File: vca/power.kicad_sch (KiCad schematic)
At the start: 16 parts, among them U16 power_conn_16, U18 LM7805_TO220, U19 ZLDO1117G33TA

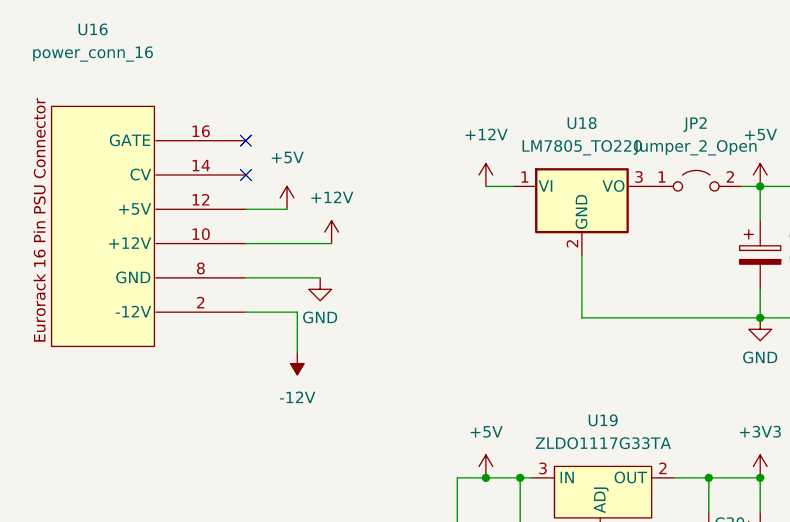
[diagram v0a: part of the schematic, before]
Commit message: added LEDs to LUM
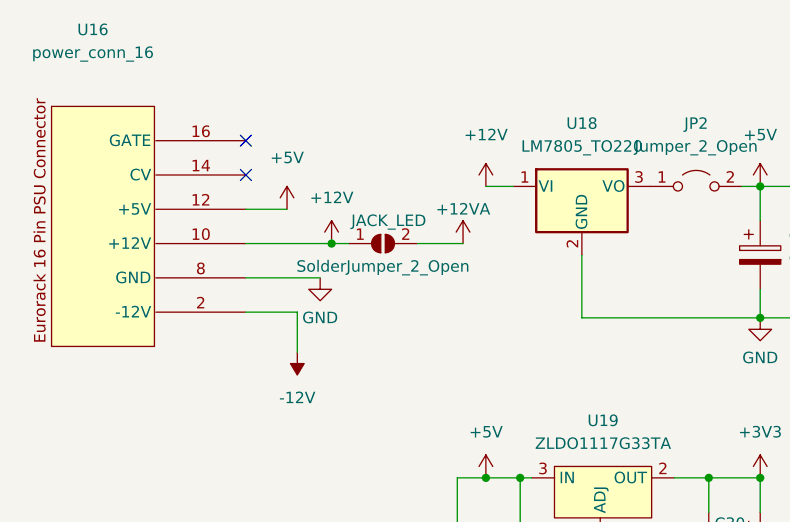
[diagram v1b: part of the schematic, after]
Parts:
- added JACK_LED: SolderJumper_2_Open, symbol Jumper:SolderJumper_2_Open
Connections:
- net +12V: now also JACK_LED.1 (A)
- new net +12VA: JACK_LED.2 (B)
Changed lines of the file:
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@@
   (junction (at 104.14 60.96) (diameter 0) (color 0 0 0 0)
+  )
+  (junction (at 62.23 34.925) (diameter 0) (color 0 0 0 0)
   )
   (junction (at 82.55 107.95) (diameter 0) (color 0 0 0 0)
@@
   )
   (wire (pts (xy 109.855 28.575) (xy 133.985 28.575))
+    (stroke (width 0) (type default) (color 0 0 0 0))
+  )
+  (wire (pts (xy 71.755 34.925) (xy 76.835 34.925))
+    (stroke (width 0) (type default) (color 0 0 0 0))
+  )
+  (wire (pts (xy 62.23 34.925) (xy 64.135 34.925))
     (stroke (width 0) (type default) (color 0 0 0 0))
   )
@@
     (pin "2")
   )
+  (symbol (lib_id "power:+12VA") (at 76.835 34.925 0) (unit 1)
+    (in_bom yes) (on_board yes)
+    (property "Reference" "#PWR?" (id 0) (at 76.835 38.735 0)
+      (effects (font (size 1.27 1.27)) hide)
+    )
+    (property "Value" "+12VA" (id 1) (at 76.835 31.115 0))
+    (property "Footprint" "" (id 2) (at 76.835 34.925 0)
+      (effects (font (size 1.27 1.27)) hide)
+    )
+    (property "Datasheet" "" (id 3) (at 76.835 34.925 0)
+      (effects (font (size 1.27 1.27)) hide)
+    )
+    (pin "1")
+  )
   (symbol (lib_id "eurorack:C-100nF-0805") (at 83.185 69.85 0) (unit 1)
     (in_bom yes) (on_board yes)
@@
     (pin "1")
   )
+  (symbol (lib_id "Jumper:SolderJumper_2_Open") (at 67.945 34.925 0) (unit 1)
+    (in_bom yes) (on_board yes)
+    (property "Reference" "JACK_LED" (id 0) (at 68.58 32.385 0))
+    (property "Value" "SolderJumper_2_Open" (id 1) (at 67.945 37.465 0))
+    (property "Footprint" "" (id 2) (at 67.945 34.925 0)
+      (effects (font (size 1.27 1.27)) hide)
+    )
+    (property "Datasheet" "~" (id 3) (at 67.945 34.925 0)
+      (effects (font (size 1.27 1.27)) hide)
+    )
+    (pin "1")
+    (pin "2")
+  )
   (symbol (lib_id "eurorack:C-100nF-0805") (at 71.755 93.98 0) (unit 1)

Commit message: some fixes, starting to work on PCB
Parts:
- JACK_LED1: renamed from JACK_LED; footprint (none) -> Jumper:SolderJumper-2_P1.3mm_Open_Pad1.0x1.5mm
- gave numbers to parts that had none: 2
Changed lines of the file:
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@@
   (symbol (lib_id "power:+12VA") (at 76.835 34.925 0) (unit 1)
     (in_bom yes) (on_board yes)
-    (property "Reference" "#PWR?" (id 0) (at 76.835 38.735 0)
+    (property "Reference" "#PWR0128" (id 0) (at 76.835 38.735 0)
       (effects (font (size 1.27 1.27)) hide)
     )
@@
   (symbol (lib_id "power:+5V") (at 155.575 62.865 0) (unit 1)
     (in_bom yes) (on_board yes) (fields_autoplaced)
-    (property "Reference" "#PWR?" (id 0) (at 155.575 66.675 0)
+    (property "Reference" "#PWR0126" (id 0) (at 155.575 66.675 0)
       (effects (font (size 1.27 1.27)) hide)
     )
@@
   (symbol (lib_id "Device:LED") (at 155.575 77.47 90) (unit 1)
     (in_bom yes) (on_board yes) (fields_autoplaced)
-    (property "Reference" "D?" (id 0) (at 158.75 77.7874 90)
+    (property "Reference" "D2" (id 0) (at 158.75 77.7874 90)
       (effects (font (size 1.27 1.27)) (justify right))
     )
@@
   (symbol (lib_id "eurorack:R-470-1206") (at 155.575 67.945 0) (unit 1)
     (in_bom yes) (on_board yes) (fields_autoplaced)
-    (property "Reference" "R?" (id 0) (at 157.48 66.6749 0)
+    (property "Reference" "R7" (id 0) (at 157.48 66.6749 0)
       (effects (font (size 1.27 1.27)) (justify left))
     )
@@
   (symbol (lib_id "Jumper:SolderJumper_2_Open") (at 67.945 34.925 0) (unit 1)
     (in_bom yes) (on_board yes)
-    (property "Reference" "JACK_LED" (id 0) (at 68.58 32.385 0))
+    (property "Reference" "JACK_LED1" (id 0) (at 68.58 32.385 0))
     (property "Value" "SolderJumper_2_Open" (id 1) (at 67.945 37.465 0))
-    (property "Footprint" "" (id 2) (at 67.945 34.925 0)
+    (property "Footprint" "Jumper:SolderJumper-2_P1.3mm_Open_Pad1.0x1.5mm" (id 2) (at 67.945 34.925 0)
       (effects (font (size 1.27 1.27)) hide)
     )
@@
   (symbol (lib_id "power:GND") (at 155.575 83.185 0) (unit 1)
     (in_bom yes) (on_board yes) (fields_autoplaced)
-    (property "Reference" "#PWR?" (id 0) (at 155.575 89.535 0)
-      (effects (font (size 1.27 1.27)) hide)
-    )
+    (property "Reference" "#PWR0127" (id 0) (at 155.575 89.535 0)
+      (effects (font (size 1.27 1.27)) hide)
+    )

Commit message: working on the back panel power section
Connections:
- net +5V: no longer C21.1
- net at JP2.1 (A), U18.3 (VO): now also C21.1
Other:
- moved on the sheet: JP2
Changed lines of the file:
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@@
 (kicad_sch (version 20211123) (generator eeschema)
   (paper "A4")
+  (junction (at 97.79 28.575) (diameter 0) (color 0 0 0 0)
+  )
   (junction (at 109.855 43.18) (diameter 0) (color 0 0 0 0)
   )
@@
   )
   (junction (at 77.47 99.06) (diameter 0) (color 0 0 0 0)
+  )
+  (junction (at 97.663 28.575) (diameter 0) (color 0 0 0 0)
   )
   (junction (at 83.185 60.96) (diameter 0) (color 0 0 0 0)
@@
     (stroke (width 0) (type default) (color 0 0 0 0))
   )
+  (wire (pts (xy 98.425 28.575) (xy 97.79 28.575))
+    (stroke (width 0) (type default) (color 0 0 0 0))
+  )
   (wire (pts (xy 100.33 60.96) (xy 104.14 60.96))
     (stroke (width 0) (type default) (color 0 0 0 0))
@@
     (stroke (width 0) (type default) (color 0 0 0 0))
   )
-  (wire (pts (xy 107.823 28.575) (xy 109.855 28.575))
+  (wire (pts (xy 108.585 28.575) (xy 109.855 28.575))
     (stroke (width 0) (type default) (color 0 0 0 0))
   )
@@
     (stroke (width 0) (type default) (color 0 0 0 0))
   )
-  (wire (pts (xy 109.855 28.575) (xy 109.855 32.385))
+  (wire (pts (xy 109.855 32.385) (xy 97.79 32.385))
     (stroke (width 0) (type default) (color 0 0 0 0))
   )
@@
     (stroke (width 0) (type default) (color 0 0 0 0))
   )
+  (wire (pts (xy 97.79 28.575) (xy 97.79 32.385))
+    (stroke (width 0) (type default) (color 0 0 0 0))
+  )
   (wire (pts (xy 104.14 64.77) (xy 104.14 60.96))
     (stroke (width 0) (type default) (color 0 0 0 0))
   )
   (wire (pts (xy 71.755 90.17) (xy 71.755 88.9))
+    (stroke (width 0) (type default) (color 0 0 0 0))
+  )
+  (wire (pts (xy 97.79 28.575) (xy 97.663 28.575))
     (stroke (width 0) (type default) (color 0 0 0 0))
   )
@@
     (pin "2")
   )
-  (symbol (lib_id "Jumper:Jumper_2_Open") (at 102.743 28.575 0) (unit 1)
-    (in_bom yes) (on_board yes) (fields_autoplaced)
-    (property "Reference" "JP2" (id 0) (at 102.743 21.59 0))
-    (property "Value" "Jumper_2_Open" (id 1) (at 102.743 24.13 0))
-    (property "Footprint" "Jumper:SolderJumper-2_P1.3mm_Open_Pad1.0x1.5mm" (id 2) (at 102.743 28.575 0)
-      (effects (font (size 1.27 1.27)) hide)
-    )
-    (property "Datasheet" "~" (id 3) (at 102.743 28.575 0)
-      (effects (font (size 1.27 1.27)) hide)
-    )
+  (symbol (lib_id "Jumper:Jumper_2_Open") (at 103.505 28.575 0) (unit 1)
+    (in_bom yes) (on_board yes) (fields_autoplaced)
+    (property "Reference" "JP2" (id 0) (at 103.505 21.59 0))
+    (property "Value" "Jumper_2_Open" (id 1) (at 103.505 24.13 0))
+    (property "Footprint" "Jumper:SolderJumper-2_P1.3mm_Open_Pad1.0x1.5mm" (id 2) (at 103.505 28.575 0)
+      (effects (font (size 1.27 1.27)) hide)
+    )
+    (property "Datasheet" "~" (id 3) (at 103.505 28.575 0)
+      (effects (font (size 1.27 1.27)) hide)
+    )

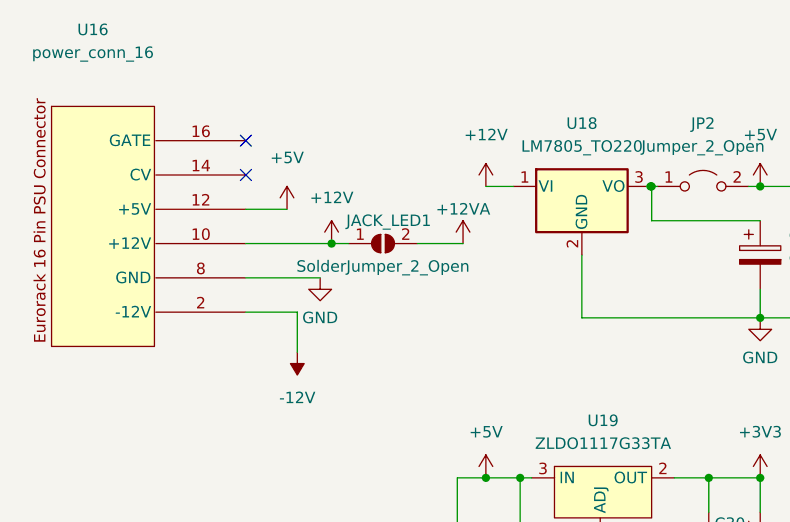
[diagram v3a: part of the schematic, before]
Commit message: Fixed some pins on the connectors, and working on the back board, power left to go
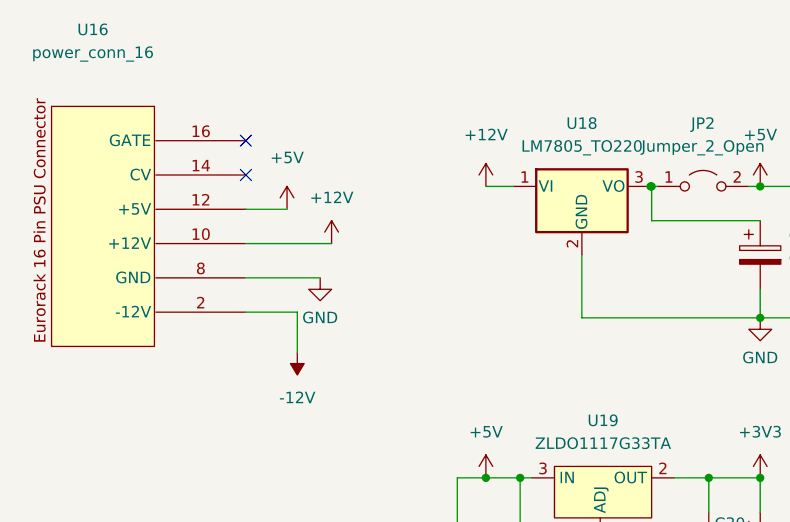
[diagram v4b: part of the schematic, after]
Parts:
- removed JACK_LED1: SolderJumper_2_Open, Jumper:SolderJumper-2_P1.3mm_Open_Pad1.0x1.5mm, symbol Jumper:SolderJumper_2_Open
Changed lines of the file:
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@@
   (junction (at 104.14 60.96) (diameter 0) (color 0 0 0 0)
-  )
-  (junction (at 62.23 34.925) (diameter 0) (color 0 0 0 0)
   )
   (junction (at 82.55 107.95) (diameter 0) (color 0 0 0 0)
@@
   )
   (wire (pts (xy 109.855 28.575) (xy 133.985 28.575))
-    (stroke (width 0) (type default) (color 0 0 0 0))
-  )
-  (wire (pts (xy 71.755 34.925) (xy 76.835 34.925))
-    (stroke (width 0) (type default) (color 0 0 0 0))
-  )
-  (wire (pts (xy 62.23 34.925) (xy 64.135 34.925))
     (stroke (width 0) (type default) (color 0 0 0 0))
   )
@@
     (pin "2")
   )
-  (symbol (lib_id "power:+12VA") (at 76.835 34.925 0) (unit 1)
-    (in_bom yes) (on_board yes)
-    (property "Reference" "#PWR0128" (id 0) (at 76.835 38.735 0)
-      (effects (font (size 1.27 1.27)) hide)
-    )
-    (property "Value" "+12VA" (id 1) (at 76.835 31.115 0))
-    (property "Footprint" "" (id 2) (at 76.835 34.925 0)
-      (effects (font (size 1.27 1.27)) hide)
-    )
-    (property "Datasheet" "" (id 3) (at 76.835 34.925 0)
-      (effects (font (size 1.27 1.27)) hide)
-    )
-    (pin "1")
-  )
   (symbol (lib_id "eurorack:C-100nF-0805") (at 83.185 69.85 0) (unit 1)
     (in_bom yes) (on_board yes)
@@
     (pin "1")
   )
-  (symbol (lib_id "Jumper:SolderJumper_2_Open") (at 67.945 34.925 0) (unit 1)
-    (in_bom yes) (on_board yes)
-    (property "Reference" "JACK_LED1" (id 0) (at 68.58 32.385 0))
-    (property "Value" "SolderJumper_2_Open" (id 1) (at 67.945 37.465 0))
-    (property "Footprint" "Jumper:SolderJumper-2_P1.3mm_Open_Pad1.0x1.5mm" (id 2) (at 67.945 34.925 0)
-      (effects (font (size 1.27 1.27)) hide)
-    )
-    (property "Datasheet" "~" (id 3) (at 67.945 34.925 0)
-      (effects (font (size 1.27 1.27)) hide)
-    )
-    (pin "1")
-    (pin "2")
-  )
   (symbol (lib_id "eurorack:C-100nF-0805") (at 71.755 93.98 0) (unit 1)

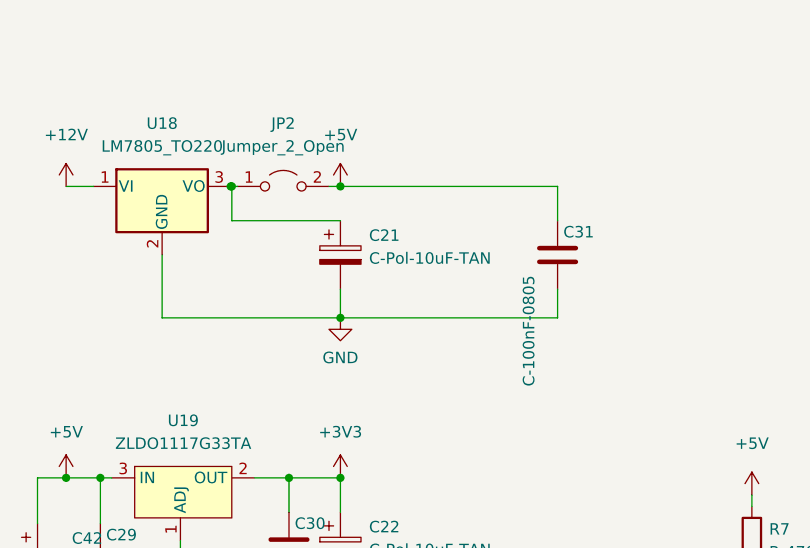
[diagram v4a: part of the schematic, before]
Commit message: Added buttons, refactored front panel, refactored power part, wip
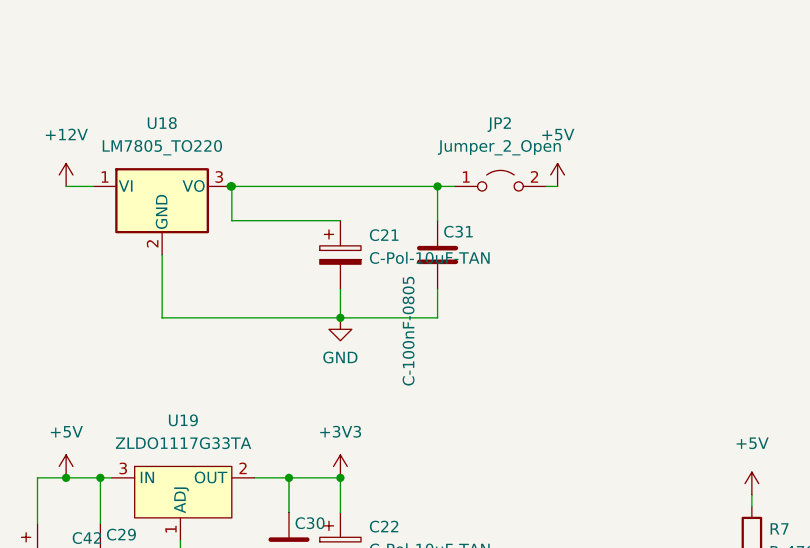
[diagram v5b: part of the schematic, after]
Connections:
- net +5V: no longer C31.1
- net at C21.1, JP2.1 (A), U18.3 (VO): now also C31.1
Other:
- moved on the sheet: C31, JP2
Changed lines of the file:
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@@
   (junction (at 109.855 75.565) (diameter 0) (color 0 0 0 0)
   )
+  (junction (at 120.65 28.575) (diameter 0) (color 0 0 0 0)
+  )
   (junction (at 77.47 99.06) (diameter 0) (color 0 0 0 0)
   )
@@
   )
   (junction (at 83.185 75.565) (diameter 0) (color 0 0 0 0)
-  )
-  (junction (at 109.855 28.575) (diameter 0) (color 0 0 0 0)
   )
   (junction (at 71.755 99.06) (diameter 0) (color 0 0 0 0)
@@
     (stroke (width 0) (type default) (color 0 0 0 0))
   )
-  (wire (pts (xy 98.425 28.575) (xy 97.79 28.575))
+  (wire (pts (xy 122.555 28.575) (xy 120.65 28.575))
     (stroke (width 0) (type default) (color 0 0 0 0))
   )
@@
     (stroke (width 0) (type default) (color 0 0 0 0))
   )
-  (wire (pts (xy 108.585 28.575) (xy 109.855 28.575))
+  (wire (pts (xy 132.715 28.575) (xy 133.985 28.575))
     (stroke (width 0) (type default) (color 0 0 0 0))
   )
@@
     (stroke (width 0) (type default) (color 0 0 0 0))
   )
-  (wire (pts (xy 109.855 43.18) (xy 133.985 43.18))
+  (wire (pts (xy 109.855 43.18) (xy 120.65 43.18))
     (stroke (width 0) (type default) (color 0 0 0 0))
   )
@@
     (stroke (width 0) (type default) (color 0 0 0 0))
   )
-  (wire (pts (xy 133.985 28.575) (xy 133.985 32.385))
+  (wire (pts (xy 120.65 28.575) (xy 120.65 32.385))
     (stroke (width 0) (type default) (color 0 0 0 0))
   )
@@
     (stroke (width 0) (type default) (color 0 0 0 0))
   )
-  (wire (pts (xy 133.985 40.005) (xy 133.985 43.18))
+  (wire (pts (xy 120.65 40.005) (xy 120.65 43.18))
+    (stroke (width 0) (type default) (color 0 0 0 0))
+  )
+  (wire (pts (xy 120.65 28.575) (xy 97.79 28.575))
     (stroke (width 0) (type default) (color 0 0 0 0))
   )
@@
   )
   (wire (pts (xy 52.705 34.925) (xy 62.23 34.925))
-    (stroke (width 0) (type default) (color 0 0 0 0))
-  )
-  (wire (pts (xy 109.855 28.575) (xy 133.985 28.575))
     (stroke (width 0) (type default) (color 0 0 0 0))
   )
@@
     (pin "1")
   )
-  (symbol (lib_id "eurorack:C-100nF-0805") (at 133.985 36.195 0) (unit 1)
+  (symbol (lib_id "eurorack:C-100nF-0805") (at 120.65 36.195 0) (unit 1)
     (in_bom yes) (on_board yes)
-    (property "Reference" "C31" (id 0) (at 134.62 33.655 0)
-      (effects (font (size 1.27 1.27)) (justify left))
-    )
-    (property "Value" "C-100nF-0805" (id 1) (at 130.81 50.8 90)
-      (effects (font (size 1.27 1.27)) (justify left))
-    )
-    (property "Footprint" "Capacitor_SMD:C_0805_2012Metric_Pad1.18x1.45mm_HandSolder" (id 2) (at 134.9502 40.005 0)
-      (effects (font (size 1.27 1.27)) hide)
-    )
-    (property "Datasheet" "https://secure.reichelt.com/at/en/smd-multilayer-ceramic-capacitor-100-n-10--x7r-g0805-100n-p31879.html?&nbc=1" (id 3) (at 133.985 36.195 0)
+    (property "Reference" "C31" (id 0) (at 121.285 33.655 0)
+      (effects (font (size 1.27 1.27)) (justify left))
+    )
+    (property "Value" "C-100nF-0805" (id 1) (at 117.475 50.8 90)
+      (effects (font (size 1.27 1.27)) (justify left))
+    )
+    (property "Footprint" "Capacitor_SMD:C_0805_2012Metric_Pad1.18x1.45mm_HandSolder" (id 2) (at 121.6152 40.005 0)
+      (effects (font (size 1.27 1.27)) hide)
+    )
+    (property "Datasheet" "https://secure.reichelt.com/at/en/smd-multilayer-ceramic-capacitor-100-n-10--x7r-g0805-100n-p31879.html?&nbc=1" (id 3) (at 120.65 36.195 0)
       (effects (font (size 1.27 1.27)) hide)
     )
@@
     (pin "2")
   )
-  (symbol (lib_id "Jumper:Jumper_2_Open") (at 103.505 28.575 0) (unit 1)
-    (in_bom yes) (on_board yes) (fields_autoplaced)
-    (property "Reference" "JP2" (id 0) (at 103.505 21.59 0))
-    (property "Value" "Jumper_2_Open" (id 1) (at 103.505 24.13 0))
-    (property "Footprint" "Jumper:SolderJumper-2_P1.3mm_Open_Pad1.0x1.5mm" (id 2) (at 103.505 28.575 0)
-      (effects (font (size 1.27 1.27)) hide)
-    )
-    (property "Datasheet" "~" (id 3) (at 103.505 28.575 0)
+  (symbol (lib_id "Jumper:Jumper_2_Open") (at 127.635 28.575 0) (unit 1)
+    (in_bom yes) (on_board yes) (fields_autoplaced)
+    (property "Reference" "JP2" (id 0) (at 127.635 21.59 0))
+    (property "Value" "Jumper_2_Open" (id 1) (at 127.635 24.13 0))
+    (property "Footprint" "Jumper:SolderJumper-2_P1.3mm_Open_Pad1.0x1.5mm" (id 2) (at 127.635 28.575 0)
+      (effects (font (size 1.27 1.27)) hide)
+    )
+    (property "Datasheet" "~" (id 3) (at 127.635 28.575 0)
       (effects (font (size 1.27 1.27)) hide)
     )
@@
     (pin "2")
   )
-  (symbol (lib_id "power:+5V") (at 109.855 28.575 0) (unit 1)
-    (in_bom yes) (on_board yes) (fields_autoplaced)
-    (property "Reference" "#PWR083" (id 0) (at 109.855 32.385 0)
-      (effects (font (size 1.27 1.27)) hide)
-    )
-    (property "Value" "+5V" (id 1) (at 109.855 22.86 0))
-    (property "Footprint" "" (id 2) (at 109.855 28.575 0)
-      (effects (font (size 1.27 1.27)) hide)
-    )
-    (property "Datasheet" "" (id 3) (at 109.855 28.575 0)
-      (effects (font (size 1.27 1.27)) hide)
-    )
+  (symbol (lib_id "power:+5V") (at 133.985 28.575 0) (unit 1)
+    (in_bom yes) (on_board yes) (fields_autoplaced)
+    (property "Reference" "#PWR083" (id 0) (at 133.985 32.385 0)
+      (effects (font (size 1.27 1.27)) hide)
+    )
+    (property "Value" "+5V" (id 1) (at 133.985 22.86 0))
+    (property "Footprint" "" (id 2) (at 133.985 28.575 0)
+      (effects (font (size 1.27 1.27)) hide)
+    )
+    (property "Datasheet" "" (id 3) (at 133.985 28.575 0)
+      (effects (font (size 1.27 1.27)) hide)
+    )
